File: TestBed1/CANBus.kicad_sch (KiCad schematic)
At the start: 6 parts, among them U2 MCP2562-E-SN

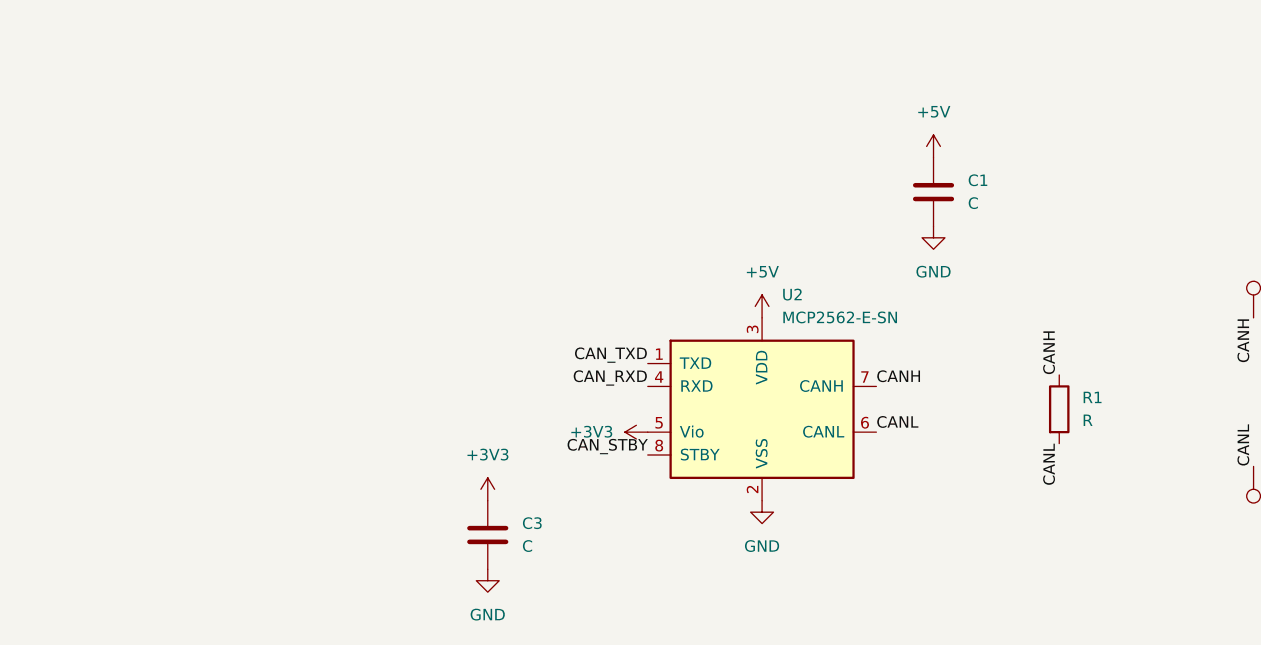
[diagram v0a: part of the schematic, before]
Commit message: Rough Grouping, Passive Footprint Assignment
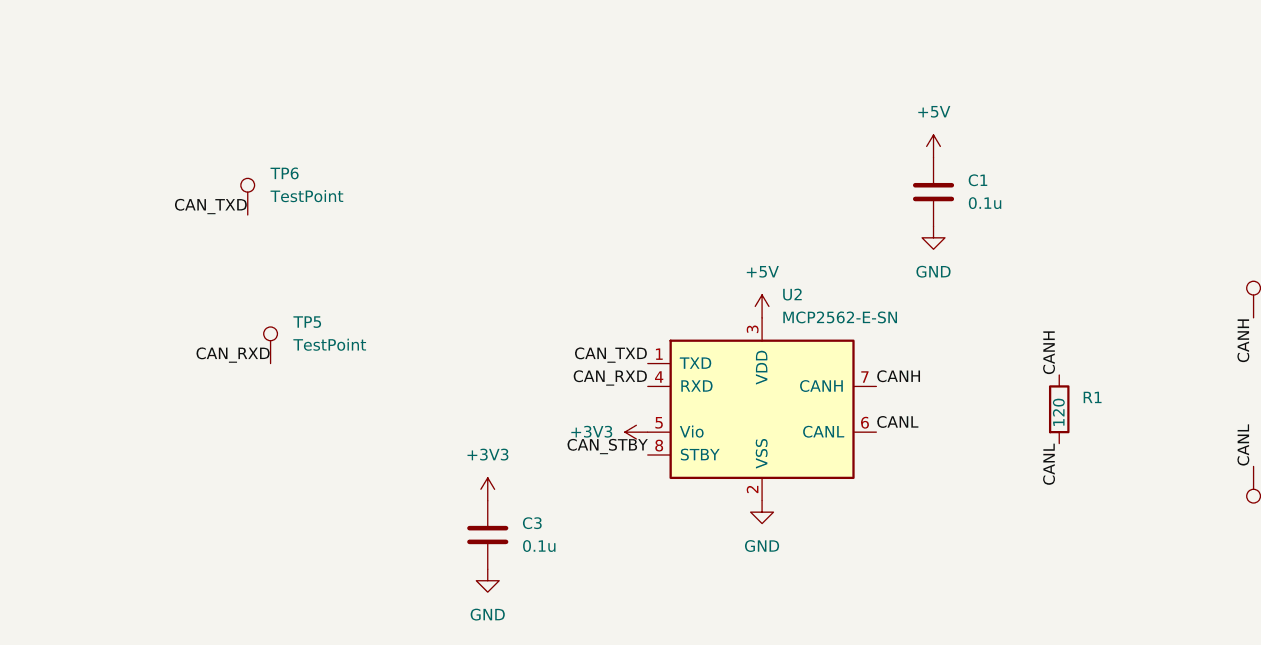
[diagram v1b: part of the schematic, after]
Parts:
- added TP5, TP6: TestPoint, TestPoint:TestPoint_Pad_1.0x1.0mm, symbol Connector:TestPoint
- C1, C3: value C -> 0.1u; footprint (none) -> Capacitor_SMD:C_0402_1005Metric_Pad0.74x0.62mm_HandSolder
- R1: value R -> 120; footprint (none) -> Resistor_SMD:R_0805_2012Metric
- TP1, TP2: footprint (none) -> TestPoint:TestPoint_Pad_1.0x1.0mm
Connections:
- net CAN_RXD: now also TP5.1
- net CAN_TXD: now also TP6.1
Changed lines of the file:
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@@
+		)
+	)
+	(label "CAN_TXD"
+		(at 87.63 57.15 180)
+		(effects
+			(font
+				(size 1.27 1.27)
+			)
+			(justify right bottom)
 		)
 	)
@@
 			)
 			(justify left bottom)
+		)
+	)
+	(label "CAN_RXD"
+		(at 90.17 73.66 180)
+		(effects
+			(font
+				(size 1.27 1.27)
+			)
+			(justify right bottom)
 		)
 	)
@@
 	)
 	(symbol
+		(lib_id "Connector:TestPoint")
+		(at 87.63 57.15 0)
+		(unit 1)
+		(exclude_from_sim no)
+		(in_bom yes)
+		(on_board yes)
+		(dnp no)
+		(fields_autoplaced yes)
+		(property "Reference" "TP6"
+			(at 90.17 52.5779 0)
+			(effects
+				(font
+					(size 1.27 1.27)
+				)
+				(justify left)
+			)
+		)
+		(property "Value" "TestPoint"
+			(at 90.17 55.1179 0)
+			(effects
+				(font
+					(size 1.27 1.27)
+				)
+				(justify left)
+			)
+		)
+		(property "Footprint" "TestPoint:TestPoint_Pad_1.0x1.0mm"
+			(at 92.71 57.15 0)
+			(effects
+				(font
+					(size 1.27 1.27)
+				)
+				(hide yes)
+			)
+		)
+		(property "Datasheet" "~"
+			(at 92.71 57.15 0)
+			(effects
+				(font
+					(size 1.27 1.27)
+				)
+				(hide yes)
+			)
+		)
+		(property "Description" "test point"
+			(at 87.63 57.15 0)
+			(effects
+				(font
+					(size 1.27 1.27)
+				)
+				(hide yes)
+			)
+		)
+		(pin "1"
+		)
+		(instances
+			(project "TestBed1"
+				(path "/1011cb81-baf2-4a82-93dd-e89e67a76dd8/3bb0df94-f6c0-4411-8c7f-d20d6a14bb72"
+					(reference "TP6")
+					(unit 1)
+				)
+			)
+		)
+	)
+	(symbol
 		(lib_id "power:+5V")
 		(at 144.78 68.58 0)
@@
 			)
 		)
-		(property "Value" "C"
+		(property "Value" "0.1u"
 			(at 118.11 93.9799 0)
 			(effects
@@
 			)
 		)
-		(property "Footprint" ""
+		(property "Footprint" "Capacitor_SMD:C_0402_1005Metric_Pad0.74x0.62mm_HandSolder"
 			(at 115.2652 96.52 0)
 			(effects
@@
 			)
 		)
-		(property "Value" "C"
+		(property "Value" "0.1u"
 			(at 167.64 55.8799 0)
 			(effects
@@
 			)
 		)
-		(property "Footprint" ""
+		(property "Footprint" "Capacitor_SMD:C_0402_1005Metric_Pad0.74x0.62mm_HandSolder"
 			(at 164.7952 58.42 0)
 			(effects
@@
 		(on_board yes)
 		(dnp no)
-		(fields_autoplaced yes)
 		(property "Reference" "R1"
 			(at 180.34 77.4699 0)
@@
 			)
 		)
-		(property "Value" "R"
-			(at 180.34 80.0099 0)
-			(effects
-				(font
-					(size 1.27 1.27)
-				)
-				(justify left)
-			)
-		)
-		(property "Footprint" ""
+		(property "Value" "120"
+			(at 177.8 80.772 90)
+			(effects
+				(font
+					(size 1.27 1.27)
+				)
+				(justify left)
+			)
+		)
+		(property "Footprint" "Resistor_SMD:R_0805_2012Metric"
 			(at 176.022 78.74 90)
 			(effects
@@
 			)
 		)
-		(property "Footprint" ""
+		(property "Footprint" "TestPoint:TestPoint_Pad_1.0x1.0mm"
 			(at 204.47 68.58 0)
 			(effects
@@
 	(symbol
 		(lib_id "Connector:TestPoint")
+		(at 90.17 73.66 0)
+		(unit 1)
+		(exclude_from_sim no)
+		(in_bom yes)
+		(on_board yes)
+		(dnp no)
+		(fields_autoplaced yes)
+		(property "Reference" "TP5"
+			(at 92.71 69.0879 0)
+			(effects
+				(font
+					(size 1.27 1.27)
+				)
+				(justify left)
+			)
+		)
+		(property "Value" "TestPoint"
+			(at 92.71 71.6279 0)
+			(effects
+				(font
+					(size 1.27 1.27)
+				)
+				(justify left)
+			)
+		)
+		(property "Footprint" "TestPoint:TestPoint_Pad_1.0x1.0mm"
+			(at 95.25 73.66 0)
+			(effects
+				(font
+					(size 1.27 1.27)
+				)
+				(hide yes)
+			)
+		)
+		(property "Datasheet" "~"
+			(at 95.25 73.66 0)
+			(effects
+				(font
+					(size 1.27 1.27)
+				)
+				(hide yes)
+			)
+		)
+		(property "Description" "test point"
+			(at 90.17 73.66 0)
+			(effects
+				(font
+					(size 1.27 1.27)
+				)
+				(hide yes)
+			)
+		)
+		(pin "1"
+		)
+		(instances
+			(project "TestBed1"
+				(path "/1011cb81-baf2-4a82-93dd-e89e67a76dd8/3bb0df94-f6c0-4411-8c7f-d20d6a14bb72"
+					(reference "TP5")
+					(unit 1)
+				)
+			)
+		)
+	)
+	(symbol
+		(lib_id "Connector:TestPoint")
 		(at 199.39 85.09 180)
 		(unit 1)
@@
 			)
 		)
-		(property "Footprint" ""
+		(property "Footprint" "TestPoint:TestPoint_Pad_1.0x1.0mm"
 			(at 194.31 85.09 0)
 			(effects

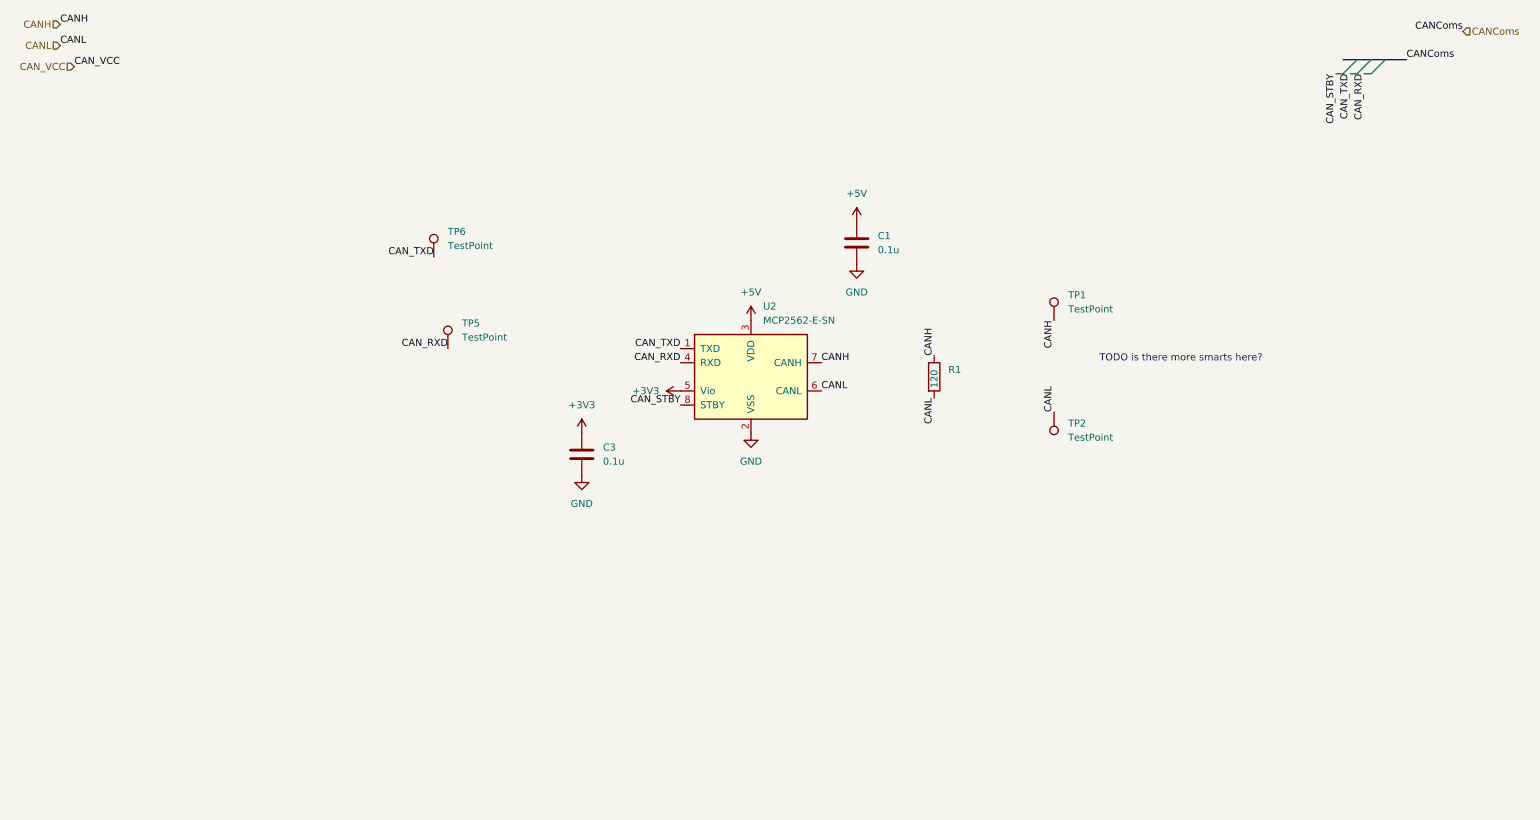
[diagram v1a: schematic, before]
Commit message: Schematic Assignment, board assignemtn and rough placement
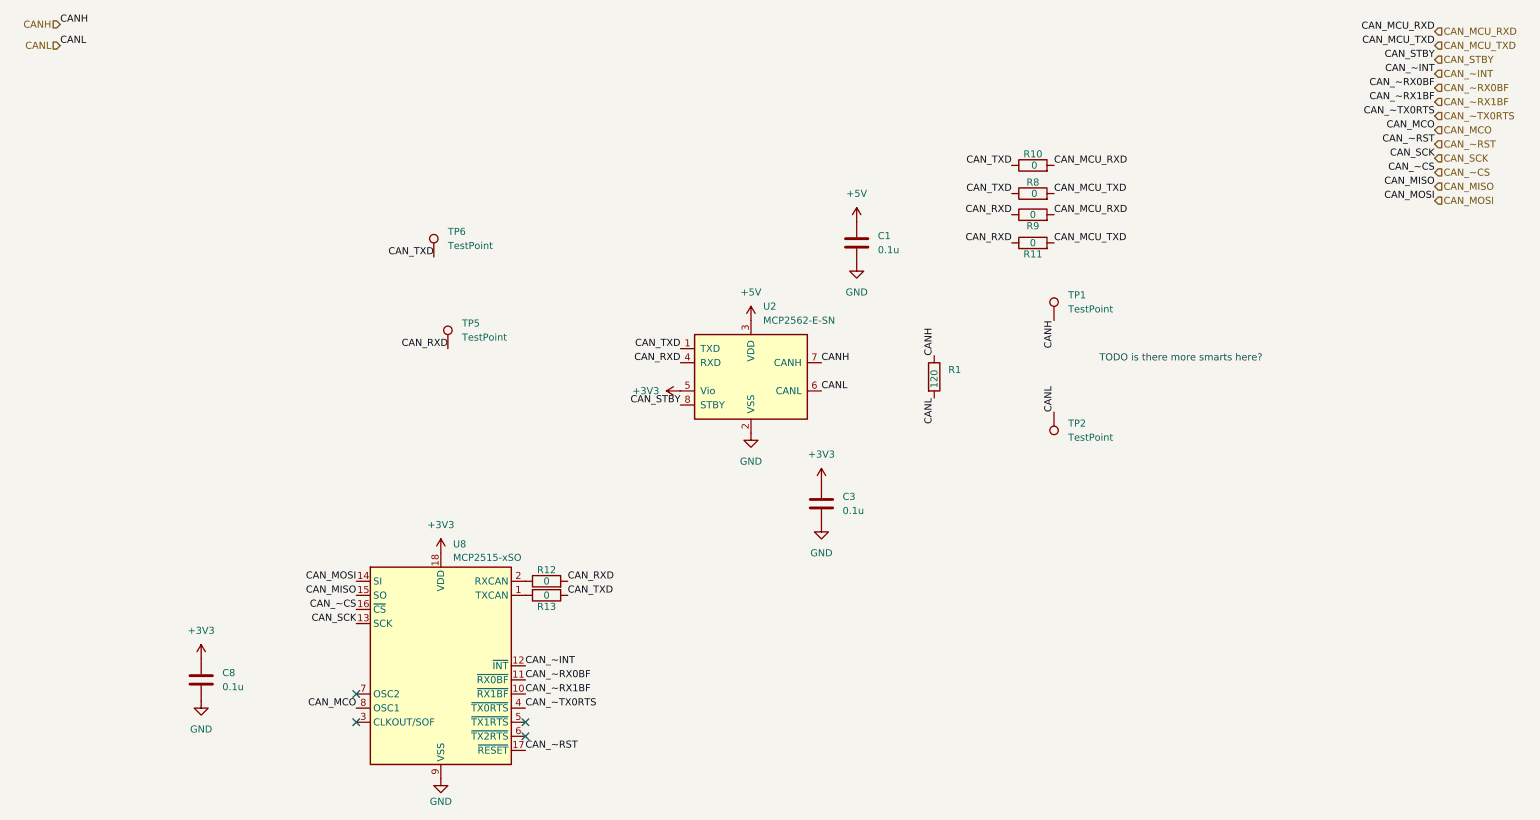
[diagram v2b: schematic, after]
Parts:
- added C8: 0.1u, Capacitor_SMD:C_0402_1005Metric_Pad0.74x0.62mm_HandSolder, symbol Device:C
- added R10, R11, R12, R13, R8, R9: 0, Resistor_SMD:R_0402_1005Metric, symbol Device:R
- added U8: MCP2515-xSO, Package_SO:SOIC-18W_7.5x11.6mm_P1.27mm, symbol Interface_CAN_LIN:MCP2515-xSO
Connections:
- net +3V3: now also C8.1, U8.18 (VDD)
- net CAN_RXD: now also R11.1, R12.2, R9.1
- net CAN_TXD: now also R10.1, R13.1, R8.1
- net GND: now also C8.2, U8.9 (VSS)
- new net: R13.2, U8.1 (TXCAN)
- new net: R12.1, U8.2 (RXCAN)
- new net CAN_MCO: U8.8 (OSC1)
- new net CAN_MCU_RXD: R10.2, R9.2
- new net CAN_MCU_TXD: R11.2, R8.2
- new net CAN_MISO: U8.15 (SO)
- new net CAN_MOSI: U8.14 (SI)
- new net CAN_SCK: U8.13 (SCK)
- new net CAN_~CS: U8.16 (~{CS})
- new net CAN_~INT: U8.12 (~{INT})
- new net CAN_~RST: U8.17 (~{RESET})
- new net CAN_~RX0BF: U8.11 (~{RX0BF})
- new net CAN_~RX1BF: U8.10 (~{RX1BF})
- new net CAN_~TX0RTS: U8.4 (~{TX0RTS})
- no-connect marks 0 -> 4
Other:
- moved on the sheet: C3
